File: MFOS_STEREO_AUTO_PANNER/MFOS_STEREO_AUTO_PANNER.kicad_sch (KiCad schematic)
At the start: 88 parts, among them U1 TL084, U2 LM13700, U3 TL082, U4 LM13700, U5 TL082, U6 LF411, U7 40106, U8 4013, U9 LF411

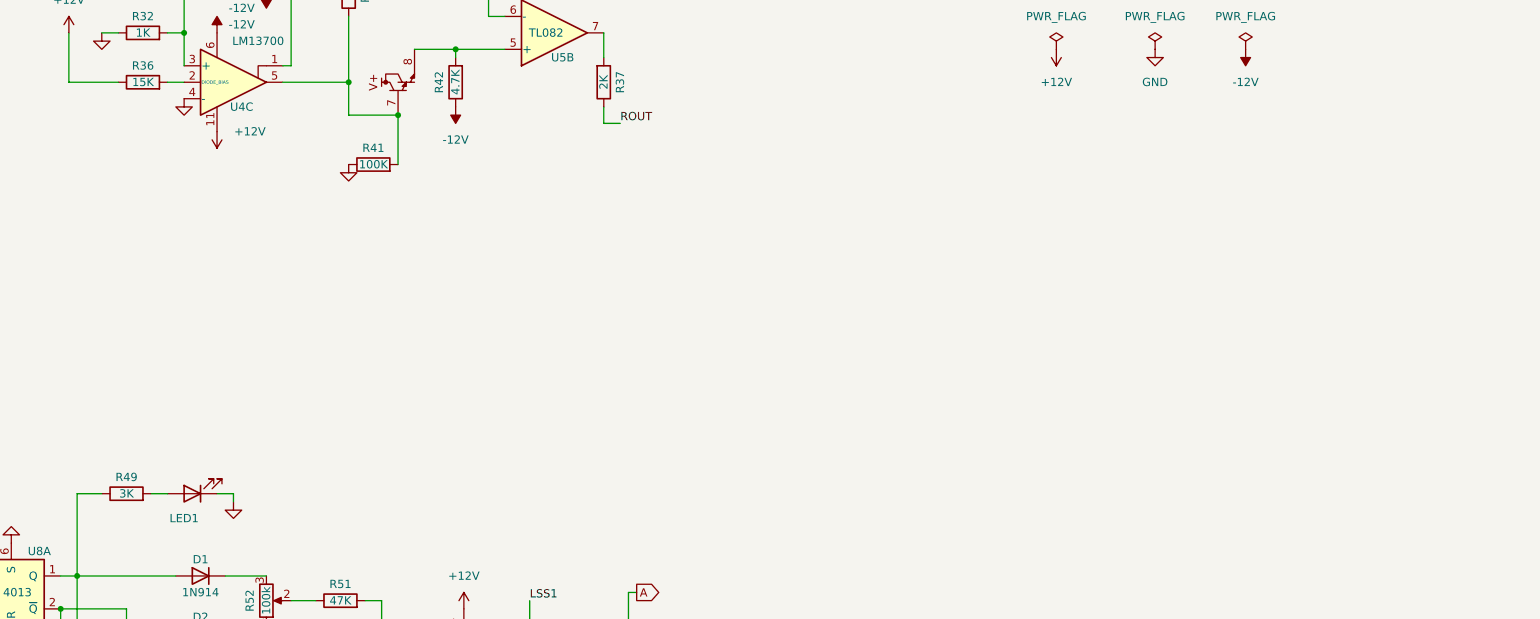
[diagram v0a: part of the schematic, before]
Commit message: Updated BOM, renamed VCO > MFOS_VCO
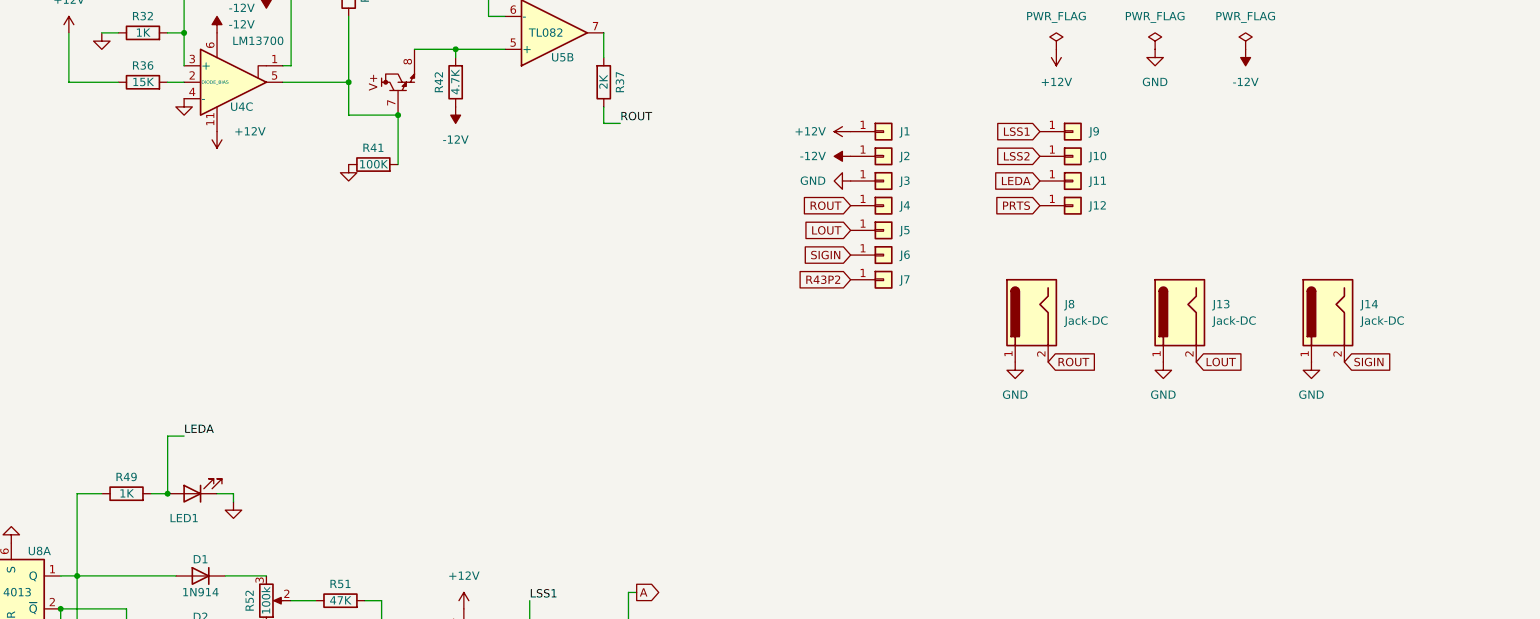
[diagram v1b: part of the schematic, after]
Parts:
- added J1, J10, J11, J12, J2, J3, J4, J5, J6, J7, J9: Conn_01x01, symbol Connector_Generic:Conn_01x01
- added J13, J14, J8: Jack-DC, symbol Connector:Jack-DC
- R49: value 3K -> 1K
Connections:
- net +12V: now also J1.1 (Pin_1)
- net -12V: now also J2.1 (Pin_1)
- net A: now also J10.1 (Pin_1)
- net GND: now also J13.1, J14.1, J3.1 (Pin_1), J8.1
- net LOUT: now also J13.2, J5.1 (Pin_1)
- net LSS1: now also J9.1 (Pin_1)
- net PRTS: now also J12.1 (Pin_1)
- net R43P2: now also J7.1 (Pin_1)
- net ROUT: now also J4.1 (Pin_1), J8.2
- net LEDA: now reaches LED1.2 (A), R49.2
- net LEDA: now also J11.1 (Pin_1)
- new net SIGIN: J14.2, J6.1 (Pin_1)

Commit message: Reviewed BOM
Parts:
- J1, J10, J11, J12, J2, J3, J4, J5, J6, J7, J9: now left out of the parts list
- R5, R52, R54, R8: symbol Device:R_Potentiometer -> Device:R_Potentiometer_Trim

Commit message: Designs adapted for BOM
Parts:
- R5, R52, R54, R8: symbol Device:R_Potentiometer_Trim -> dhk:R_Potentiometer_Trim
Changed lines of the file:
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@@
     (pin "7")
   )
-  (symbol (lib_id "Device:R_Potentiometer_Trim") (at 157.48 31.75 90) (unit 1)
+  (symbol (lib_id "dhk:R_Potentiometer_Trim") (at 157.48 31.75 90) (unit 1)
     (in_bom yes) (on_board yes)
     (property "Reference" "R5" (id 0) (at 157.48 34.29 90))
@@
     (pin "1")
   )
-  (symbol (lib_id "Device:R_Potentiometer_Trim") (at 55.88 33.02 90) (unit 1)
+  (symbol (lib_id "dhk:R_Potentiometer_Trim") (at 55.88 33.02 90) (unit 1)
     (in_bom yes) (on_board yes)
     (property "Reference" "R8" (id 0) (at 55.88 35.56 90))
@@
     (pin "1")
   )
-  (symbol (lib_id "Device:R_Potentiometer_Trim") (at 171.45 181.61 0) (mirror x) (unit 1)
+  (symbol (lib_id "dhk:R_Potentiometer_Trim") (at 171.45 181.61 0) (mirror x) (unit 1)
     (in_bom yes) (on_board yes)
     (property "Reference" "R52" (id 0) (at 168.91 181.61 90))
@@
     (pin "1")
   )
-  (symbol (lib_id "Device:R_Potentiometer_Trim") (at 171.45 199.39 0) (mirror x) (unit 1)
+  (symbol (lib_id "dhk:R_Potentiometer_Trim") (at 171.45 199.39 0) (mirror x) (unit 1)
     (in_bom yes) (on_board yes)
     (property "Reference" "R54" (id 0) (at 168.91 199.39 90))
